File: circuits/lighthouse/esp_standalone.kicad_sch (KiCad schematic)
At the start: 22 parts, among them Q1 SS8050, Q2 SS8050, U1 AMS1117-3.3, U2 CP2102-GMR, U3 ESP32-WROOM-32

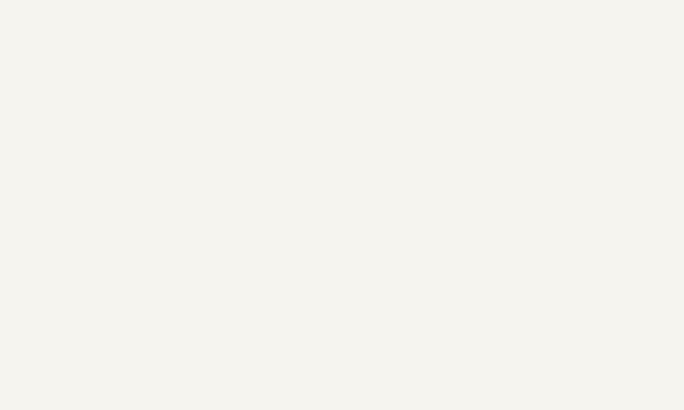
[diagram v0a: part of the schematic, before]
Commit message: The circuit now has all the values in place
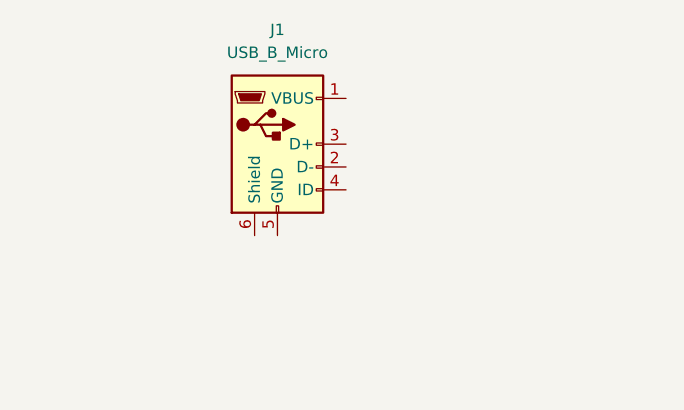
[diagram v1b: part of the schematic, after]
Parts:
- added J1: USB_B_Micro, symbol Connector:USB_B_Micro
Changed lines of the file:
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@@
+	)
+	(symbol
+		(lib_id "Connector:USB_B_Micro")
+		(at 49.53 45.72 0)
+		(unit 1)
+		(exclude_from_sim no)
+		(in_bom yes)
+		(on_board yes)
+		(dnp no)
+		(fields_autoplaced yes)
+		(property "Reference" "J1"
+			(at 49.53 33.02 0)
+			(effects
+				(font
+					(size 1.27 1.27)
+				)
+			)
+		)
+		(property "Value" "USB_B_Micro"
+			(at 49.53 35.56 0)
+			(effects
+				(font
+					(size 1.27 1.27)
+				)
+			)
+		)
+		(property "Footprint" ""
+			(at 53.34 46.99 0)
+			(effects
+				(font
+					(size 1.27 1.27)
+				)
+				(hide yes)
+			)
+		)
+		(property "Datasheet" "~"
+			(at 53.34 46.99 0)
+			(effects
+				(font
+					(size 1.27 1.27)
+				)
+				(hide yes)
+			)
+		)
+		(property "Description" "USB Micro Type B connector"
+			(at 49.53 45.72 0)
+			(effects
+				(font
+					(size 1.27 1.27)
+				)
+				(hide yes)
+			)
+		)
+		(pin "2"
+		)
+		(pin "3"
+		)
+		(pin "1"
+		)
+		(pin "4"
+		)
+		(pin "6"
+		)
+		(pin "5"
+		)
+		(instances
+			(project ""
+				(path "/fdc09105-4d8a-4d73-bf3d-91ae578d21e8"
+					(reference "J1")
+					(unit 1)
+				)
+			)
+		)
 	)
 	(symbol
